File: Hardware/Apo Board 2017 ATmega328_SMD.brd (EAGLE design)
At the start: 78.7 x 48.7 mm, 29 parts, among them U1 LED-TRICOLOR-5050-IC, U10 LED-TRICOLOR-5050-IC, U11 LED-TRICOLOR-5050-IC, U2 ATMEGA328P_PDIP, U3 LED-TRICOLOR-5050-IC, U4 LED-TRICOLOR-5050-IC, U5 LED-TRICOLOR-5050-IC, U6 LED-TRICOLOR-5050-IC, U7 LED-TRICOLOR-5050-IC, U8 LED-TRICOLOR-5050-IC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

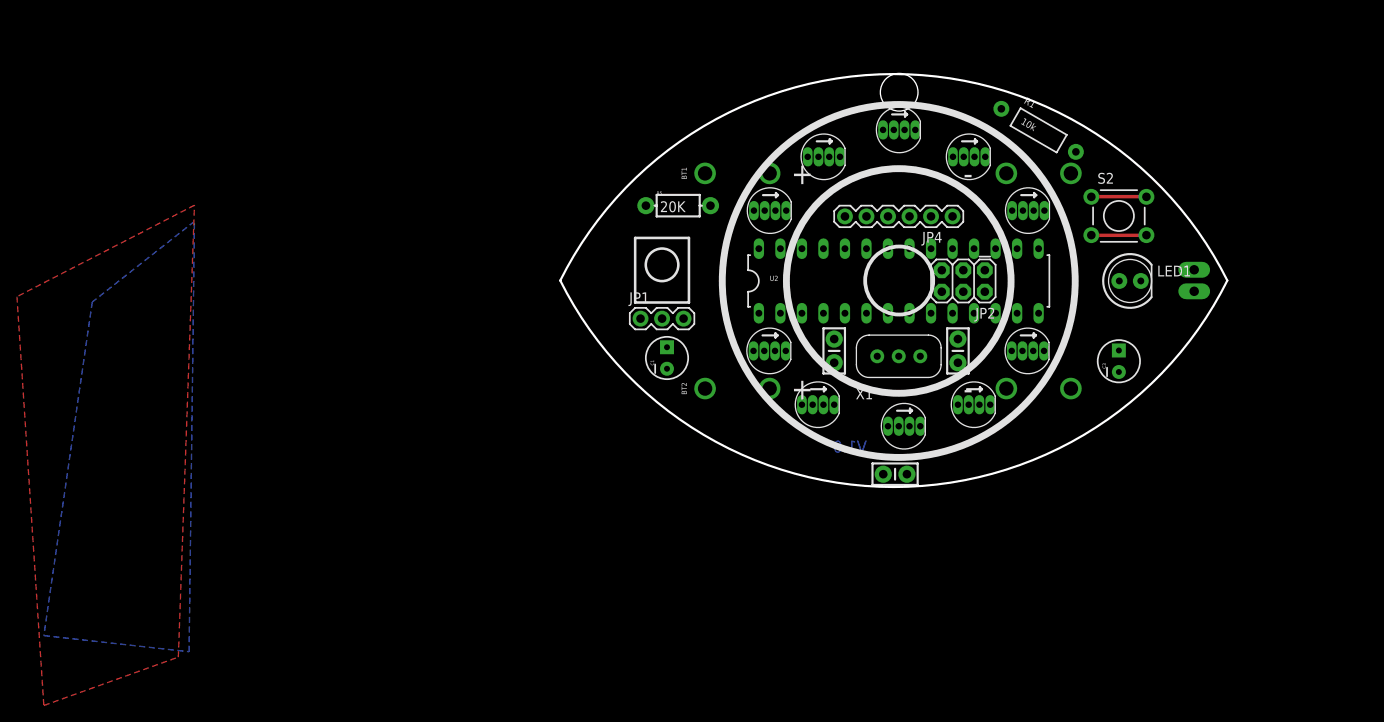
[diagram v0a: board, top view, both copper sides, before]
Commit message: Adding ATmega328 versions
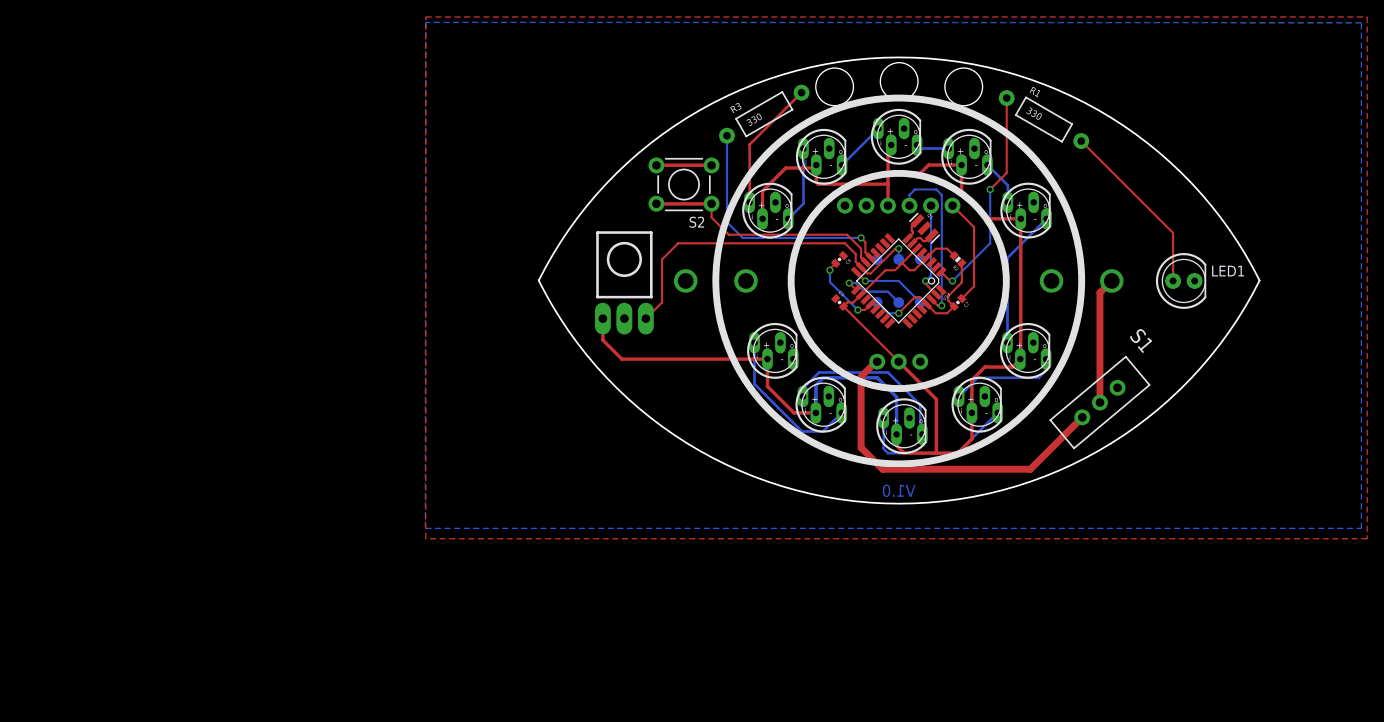
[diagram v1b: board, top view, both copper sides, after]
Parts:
- removed 0.1UF: (no value), SparkFun-Capacitors:CAP-PTH-SMALL-KIT
- removed BT1, BT2: (no value), SparkFun-Batteries:BATTERY-AAA
- removed C3: (no value), SparkFun-Capacitors:CPOL-RADIAL-10UF-25V
- removed C5: 4.7uF, SparkFun-Passives:CAP-PTH-SMALL-KIT
- removed C6: 0.1uF, SparkFun-Passives:CAP-PTH-SMALL-KIT
- removed JP2: ISP, SparkFun:2X3
- removed R5: 20K, SparkFun-Passives:AXIAL-0.3-KIT
- removed U2: ATMEGA328P_PDIP, SparkFun-DigitalIC:DIL28-3
- removed X1: 16Mhz, 1_Dan Master:CERAMIC_RESONATOR_ZTT
- added BAT1: AA, SparkFun:BATTERY-AA-KIT
- added C4, C7: 0.1uF, SparkFun:0402-CAP
- added Q1: RESONATORSMD, SparkFun:RESONATOR-SMD
- added R2: 10K, SparkFun:0402-RES
- added R3: 330, SparkFun-Resistors:AXIAL-0.4
- added S1: (no value), SparkFun:SWITCH-SPDT_KIT
- added TP1, TP2, TP3, TP4, TP5, TP6: TP-3x5, SparkFun-Passives:PAD.03X.05
- added U13: ATMEGA328, SparkFun:TQFP32-08
- C1: value 1000uF -> 0.1uF; device SparkFun-Capacitors:CPOL-RADIAL-10UF-25V -> SparkFun:0402-CAP
- JP1: device SparkFun-Connectors:1X03 -> SparkFun-Connectors:1X03_IR_RECEIVER
- JP3: value M02PTH3 -> NCP1402; device SparkFun-Connectors:1X02_LONGPADS -> SparkFun-Connectors:1X03_BOOST
- R1: value 10k -> 330
- moved S2 51.5 mm to (-25.3, 11.4), turned to 180 degrees
- moved JP3 35.8 mm to (0.00, -9.53), turned to 0 degrees
- moved C1 21.4 mm to (-6.99, -2.54), turned to 315 degrees
- moved FRAME1 10.8 mm to (-21.8, -39.7)
- moved LED1 6.35 mm to (33.7, 0.00)
- moved JP1 1.90 mm to (-32.4, -4.45)
- moved R1 1.42 mm to (17.1, 19.1)
- moved JP4 1.27 mm to (6.35, 8.89), flipped to the bottom, turned to 0 degrees
- moved U5 0.81 mm to (0.00, 17.0)
- moved U1 0.63 mm to (-8.89, -14.6)
- moved U10 0.63 mm to (9.53, -14.6)
- moved U8 0.63 mm to (-14.6, -8.26)
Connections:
- removed net +: BT1.PWR@1, BT2.PWR@1
- removed net -: BT1.GND@1, BT2.GND@1
- removed net BUTTON_PIN: S2.1, S2.2, U2.4
- removed net IR_RECEIVE: JP1.3
- removed net N$10: C6.2, R5.P$1, U2.1
- removed net N$12: U2.5
- removed net N$21: U2.16
- removed net VCC: 0.1UF.1, C1.1
- removed net VREG: C3.1, JP3.2
- new net AREF: C4.2, U13.20
- new net BUTTON: S2.1, S2.2, U13.14
- new net N$29: Q1.1, U13.8
- new net N$30: Q1.3, U13.7
- new net N$8: JP3.1, S1.3
- net +5V: now also C1.2, JP3.2, R2.2, TP1.P$1, U13.18, U13.4, U13.6; no longer C5.1, JP2.2, R5.P$2, U2.20, U2.21, U2.7
- net DTR: now also C7.1; no longer C6.1
- net GND: now also BAT1.GND@1, C1.1, C4.1, JP3.3, Q1.2, TP3.P$1, U13.21, U13.3, U13.5; no longer 0.1UF.2, C1.2, C3.2, C5.2, JP2.6, JP3.1, U2.22, U2.8, X1.P$2
- net IR_SEND: now also U13.1
- net LED_PIN: now also R3.P$2
- net MISO: now also TP4.P$1, U13.16; no longer JP2.1, U2.18
- net MOSI: now also JP1.3, TP2.P$1, U13.15; no longer JP2.4, U2.17
- net N$15: now also U13.2; no longer U2.6
- net N$16: now also U13.9; no longer U2.11
- net N$17: now also U13.10; no longer U2.12
- net N$18: now also U13.11; no longer U2.13
- net N$19: now also U13.12; no longer U2.14
- net N$20: now also R3.P$1, U13.13; no longer U2.15
- net N$22: now also U13.28; no longer U2.28
- net N$23: now also U13.27; no longer U2.27
- net N$24: now also U13.26; no longer U2.26
- net N$25: now also U13.25; no longer U2.25
- net N$26: now also U13.24; no longer U2.24
- net N$27: now also U13.23; no longer U2.23
- net N$4: now also U13.32; no longer U2.9, X1.P$1
- net N$7: now also BAT1.PWR@1, S1.2; no longer U2.10, X1.P$3
- net RESET: now also C7.2, R2.1, TP6.P$1, U13.29; no longer JP2.5
- net RX: now also U13.30; no longer U2.2
- net SCK: now also TP5.P$1, U13.17; no longer JP2.3, U2.19
- net TX: now also U13.31; no longer U2.3
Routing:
- net +5V: track 0.00 -> 183.9 mm
- net MOSI: track 0.00 -> 41.0 mm, vias 0 -> 1
- net N$8: track 0.00 -> 40.7 mm
- net N$20: track 0.00 -> 29.6 mm, vias 0 -> 1
- net BUTTON: track 0.00 -> 29.2 mm
- net IR_SEND: track 0.00 -> 26.0 mm, vias 0 -> 2
- net N$3: track 0.00 -> 21.0 mm
- net N$13: track 0.00 -> 20.9 mm
- net RX: track 0.00 -> 20.2 mm, vias 0 -> 1
- net N$11: track 0.00 -> 19.3 mm
- net N$14: track 0.00 -> 18.4 mm
- net RESET: track 0.00 -> 17.5 mm, vias 0 -> 1
- net DOUT_DIN: track 0.00 -> 16.5 mm
- net LED_PIN: track 0.00 -> 15.5 mm
- net N$7: track 0.00 -> 14.9 mm
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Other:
- board size 78.7 x 48.7 mm -> 85.1 x 52.7 mm
- board text added: "BLK"
- board text added: "GRN"
- board text added: "Joel Bartlett"

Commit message: Cleanup
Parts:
- moved LOGO1 128.3 mm to (30.5, -6.30)
- moved S1 1.91 mm to (23.7, -12.4)
- moved R1 0.90 mm to (16.5, 19.7)
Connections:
- net GND: now also JP3.1; no longer JP3.3
- net N$8: now also JP3.3; no longer JP3.1
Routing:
- net N$8: track 40.7 -> 21.1 mm
- net N$9: track 12.9 -> 21.2 mm, vias 0 -> 1
- net +5V: track 183.9 -> 175.9 mm, vias 0 -> 1
- net N$7: track 14.9 -> 13.0 mm
- net N$11: track 19.3 -> 20.5 mm
- net N$3: track 21.0 -> 21.9 mm
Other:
- board text added: "MODE"
- board text added: "ON/OFF"
- board text added: "V0.1"
- board text added: "https://github.com/apoboard"
- board text removed: "V1.0"

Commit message: Power Tests
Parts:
- added BAT2: AA, SparkFun:BATTERY-AA-KIT
- moved BAT1 10.2 mm to (0.00, -10.2)
- moved U8 4.26 mm to (-16.5, -4.45)
- moved U11 2.84 mm to (16.5, -5.71)
- moved U4 2.84 mm to (16.6, 5.77)
- moved U7 2.84 mm to (-16.5, 5.77)
- moved U1 2.69 mm to (-10.8, -12.7)
- moved U3 2.01 mm to (10.2, 14.0)
- moved U6 2.01 mm to (-10.7, 14.0)
- moved U10 1.42 mm to (10.2, -13.3)
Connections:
- new net N$10: BAT1.PWR@1, BAT2.GND@1
- net N$7: now also BAT2.PWR@1; no longer BAT1.PWR@1
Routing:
- net +5V: track 175.9 -> 190.8 mm
- net N$7: track 13.0 -> 0.00 mm
- net N$14: track 18.4 -> 23.4 mm
- net N$9: track 21.2 -> 25.2 mm
- net DOUT_DIN: track 16.5 -> 13.8 mm
- net LED_PIN: track 15.5 -> 18.1 mm
- net N$1: track 9.02 -> 11.5 mm
- net N$5: track 3.91 -> 5.85 mm
- net N$2: track 6.07 -> 7.91 mm
- net N$11: track 20.5 -> 21.8 mm
- net N$6: track 5.41 -> 6.56 mm
- net N$13: track 21.1 -> 22.1 mm
